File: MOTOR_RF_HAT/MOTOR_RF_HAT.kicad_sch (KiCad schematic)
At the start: 31 parts, among them J1 Conn_01x01, J2 Conn_01x01, Q1 BSS138, U1 XT30PW-M, U2 LMR51420YFDDCR

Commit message: MOTOR_RF_HAT: BOM enrichment + design review fixes + firmware scaffold
BOM enrichment:
- Added LCSC, MPN, and Farnell properties to 122 of 131 components
  across all schematic sheets (remaining 9 are mechanical/test fixtures)
- Sourced all passives (0603 caps/resistors/inductors), ICs (CC1200,
  A4950E, LMR51420, BSS138, WS2812B), connectors (JST-XH, XT30, SMA)

Design review fixes:
- C1 (4.7uF 50V): 0805→1206 (physically impossible in 0805)
- R1/R2: fixed footprint library from Capacitor_SMD to Resistor_SMD

Firmware scaffold (Firmware/rp2040-motor-rf-hat/):
- Complete merged firmware: RF HAT base + rotator motor control
- motor_pwm.cpp refactored for 2-pin A4950 (IN1/IN2, no PWM pin)
- adxl345.cpp with SPI0 mode switching (mode 3 for IMU, mode 0 for VHF)
- proto.c extended with motor messages 0x60-0x69 (SET_POSITION, PARK,
  STOP, HOME, GET_STATUS, SET_GAINS, ZERO, IMU_READ, RECAL)
- Builds clean: 5.7% RAM, 4.2% flash
- Output: motor_rf_hat_firmware.uf2

Co-Authored-By: Claude Opus 4.6 (1M context) <noreply@anthropic.com>
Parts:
- C1: footprint Capacitor_SMD:C_0805_2012Metric -> Capacitor_SMD:C_1206_3216Metric
- D2, D4, D5, D6: LCSC (none) -> C965555; MPN (none) -> WS2812B-2020
- D3: Farnell (none) -> 1612348; LCSC (none) -> C2128; MPN (none) -> 1N4148WS
- Q1: Farnell (none) -> 9845330; LCSC (none) -> C112239; MPN (none) -> BSS138
- R1, R2: footprint Capacitor_SMD:C_0603_1608Metric -> Resistor_SMD:R_0603_1608Metric
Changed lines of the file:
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@@
 			)
 		)
-		(property "Footprint" "Capacitor_SMD:C_0603_1608Metric"
+		(property "Footprint" "Resistor_SMD:R_0603_1608Metric"
 			(at 121.158 38.1 90)
 			(hide yes)
@@
 			)
 		)
+		(property "LCSC" "C965555"
+			(at 0 0 0)
+			(show_name no)
+			(do_not_autoplace no)
+			(hide yes)
+			(effects
+				(font
+					(size 1.27 1.27)
+				)
+			)
+		)
+		(property "MPN" "WS2812B-2020"
+			(at 0 0 0)
+			(show_name no)
+			(do_not_autoplace no)
+			(hide yes)
+			(effects
+				(font
+					(size 1.27 1.27)
+				)
+			)
+		)
 		(pin "3"
 		)
@@
 			)
 		)
+		(property "LCSC" "C965555"
+			(at 0 0 0)
+			(hide yes)
+			(show_name no)
+			(do_not_autoplace no)
+			(effects (font (size 1.27 1.27)))
+		)
+		(property "MPN" "WS2812B-2020"
+			(at 0 0 0)
+			(hide yes)
+			(show_name no)
+			(do_not_autoplace no)
+			(effects (font (size 1.27 1.27)))
+		)
 		(pin "3"
 		)
@@
 			)
 		)
-		(property "Footprint" "Capacitor_SMD:C_0603_1608Metric"
+		(property "Footprint" "Resistor_SMD:R_0603_1608Metric"
 			(at 117.602 48.26 90)
 			(hide yes)
@@
 			)
 		)
+		(property "LCSC" "C2128"
+			(at 0 0 0)
+			(hide yes)
+			(show_name no)
+			(do_not_autoplace no)
+			(effects (font (size 1.27 1.27)))
+		)
+		(property "MPN" "1N4148WS"
+			(at 0 0 0)
+			(hide yes)
+			(show_name no)
+			(do_not_autoplace no)
+			(effects (font (size 1.27 1.27)))
+		)
+		(property "Farnell" "1612348"
+			(at 0 0 0)
+			(hide yes)
+			(show_name no)
+			(do_not_autoplace no)
+			(effects (font (size 1.27 1.27)))
+		)
 		(pin "2"
 		)
@@
 			)
 		)
+		(property "LCSC" "C965555"
+			(at 0 0 0)
+			(hide yes)
+			(show_name no)
+			(do_not_autoplace no)
+			(effects (font (size 1.27 1.27)))
+		)
+		(property "MPN" "WS2812B-2020"
+			(at 0 0 0)
+			(hide yes)
+			(show_name no)
+			(do_not_autoplace no)
+			(effects (font (size 1.27 1.27)))
+		)
 		(pin "3"
 		)
@@
 			)
 		)
-		(property "Footprint" "Capacitor_SMD:C_0805_2012Metric"
+		(property "Footprint" "Capacitor_SMD:C_1206_3216Metric"
 			(at 45.4152 45.72 0)
 			(hide yes)
@@
 			)
 		)
+		(property "LCSC" "C112239"
+			(at 0 0 0)
+			(hide yes)
+			(show_name no)
+			(do_not_autoplace no)
+			(effects (font (size 1.27 1.27)))
+		)
+		(property "MPN" "BSS138"
+			(at 0 0 0)
+			(hide yes)
+			(show_name no)
+			(do_not_autoplace no)
+			(effects (font (size 1.27 1.27)))
+		)
+		(property "Farnell" "9845330"
+			(at 0 0 0)
+			(hide yes)
+			(show_name no)
+			(do_not_autoplace no)
+			(effects (font (size 1.27 1.27)))
+		)
 		(pin "3"
 		)
@@
 			)
 		)
+		(property "LCSC" "C965555"
+			(at 0 0 0)
+			(hide yes)
+			(show_name no)
+			(do_not_autoplace no)
+			(effects (font (size 1.27 1.27)))
+		)
+		(property "MPN" "WS2812B-2020"
+			(at 0 0 0)
+			(hide yes)
+			(show_name no)
+			(do_not_autoplace no)
+			(effects (font (size 1.27 1.27)))
+		)
 		(pin "3"

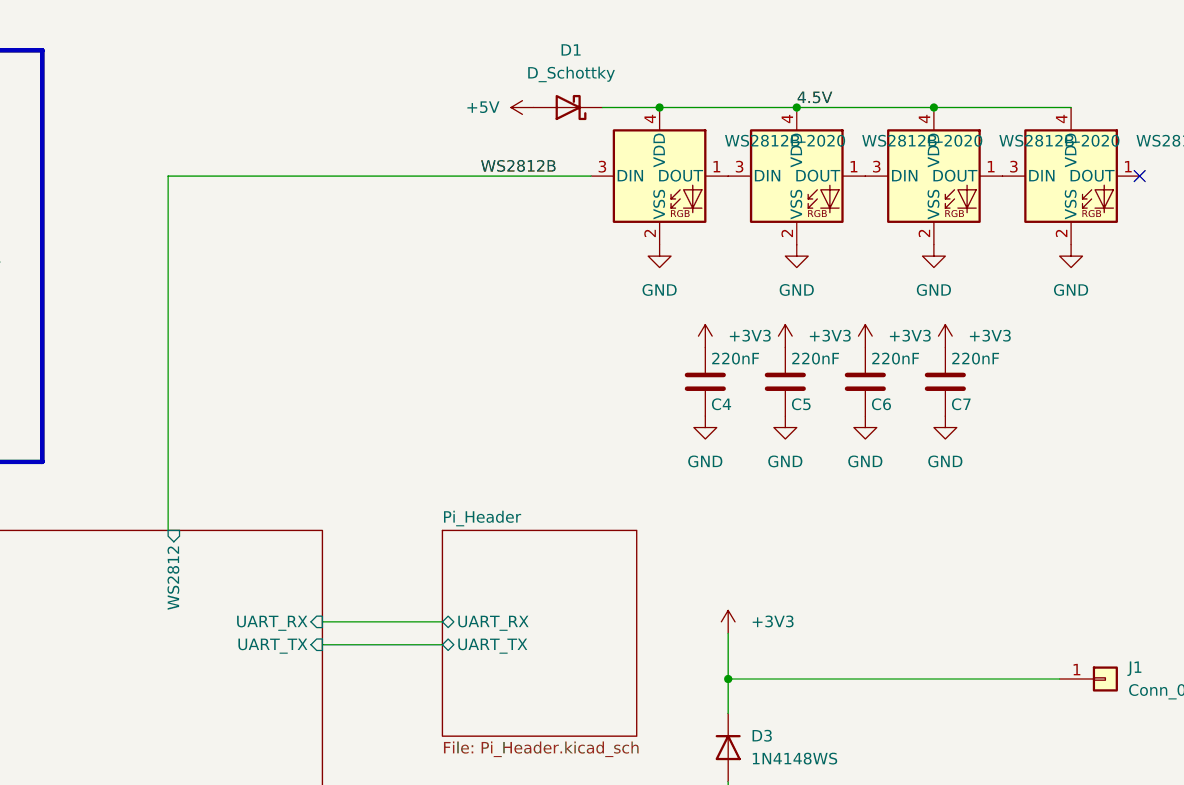
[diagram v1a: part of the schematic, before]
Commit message: MOTOR_RF_HAT: final production check — BOM fix + routed PCB
BOM fix:
- A4950 VBB bypass caps (C60-C62, C64-C66): changed MPN from
  CL10A106KP8NNNC (10uF/10V 0603, WRONG) to CL21A106KPFNNNE
  (10uF/10V 0805). Note: for 24V bus these should ideally be
  50V-rated — verify before ordering.

ERC: 47 violations (4 errors, 43 warnings)
- All 4 errors are false positives (power pin connectivity
  through Schottky diode, Pico dual-ground, cross-sheet power)
- 43 warnings are pre-existing from RF_HAT base design

Production readiness:
- All symbols resolve (5 local + 15 KiCad global)
- All footprints resolve (5 local + 19 KiCad global)
- All 3D models resolve (20 in PCB, 9 in footprints)
- BOM enriched: 122/131 components have LCSC + MPN + Farnell
- Firmware builds clean: 5.7% RAM, 4.2% flash

Before ordering:
- [ ] Run Update PCB from Schematic (new motor/encoder nets)
- [ ] Verify A4950 VBB cap voltage rating (need 50V for 24V bus)
- [ ] Add bulk 470µF electrolytic externally
- [ ] VNA tune VHF matching network post-assembly

Co-Authored-By: Claude Opus 4.6 (1M context) <noreply@anthropic.com>
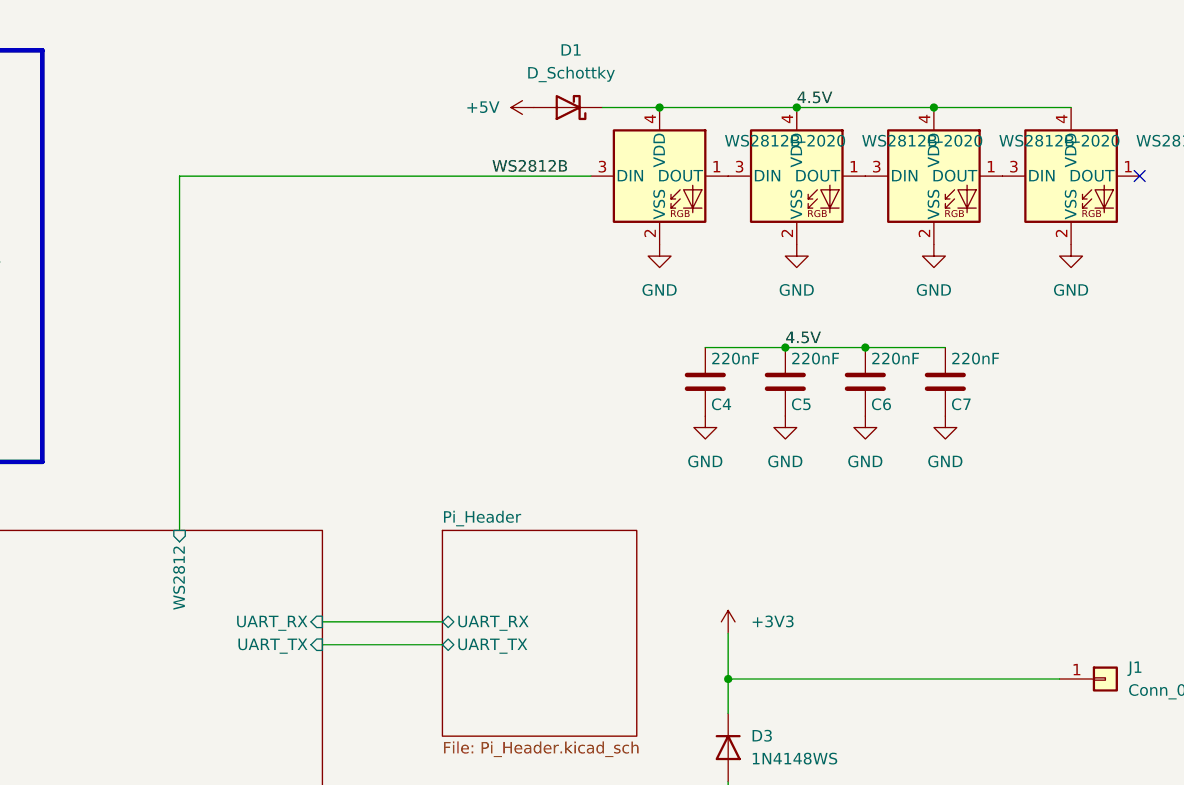
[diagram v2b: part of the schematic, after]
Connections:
- net +3V3: no longer C4.1, C5.1, C6.1, C7.1
- net 4.5V: now also C4.1, C5.1, C6.1, C7.1
